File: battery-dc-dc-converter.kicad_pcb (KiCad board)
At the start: 2 copper layers, 42 x 33 mm, 24 parts, among them J1 Conn_01x02, J2 Conn_01x01, J3 Conn_01x01, U1 LMR16030

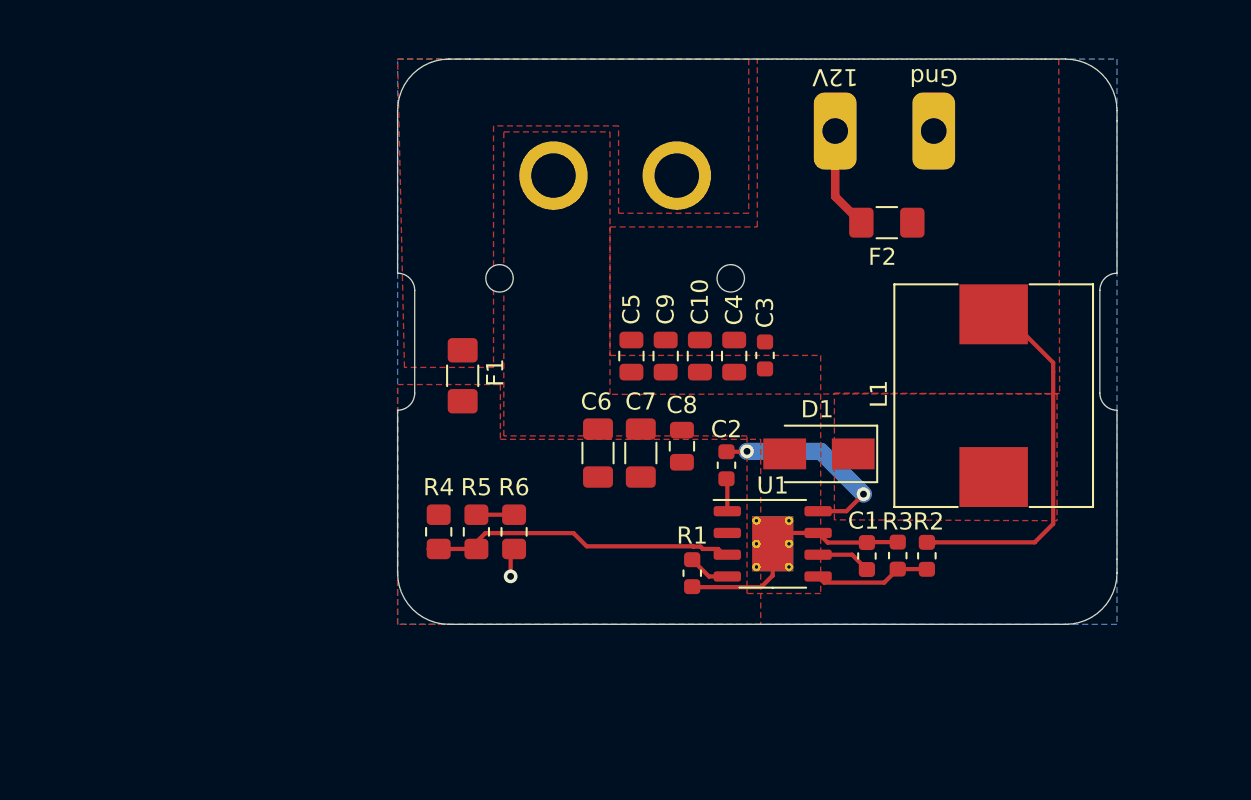
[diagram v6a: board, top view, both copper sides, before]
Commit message: Improved EMI
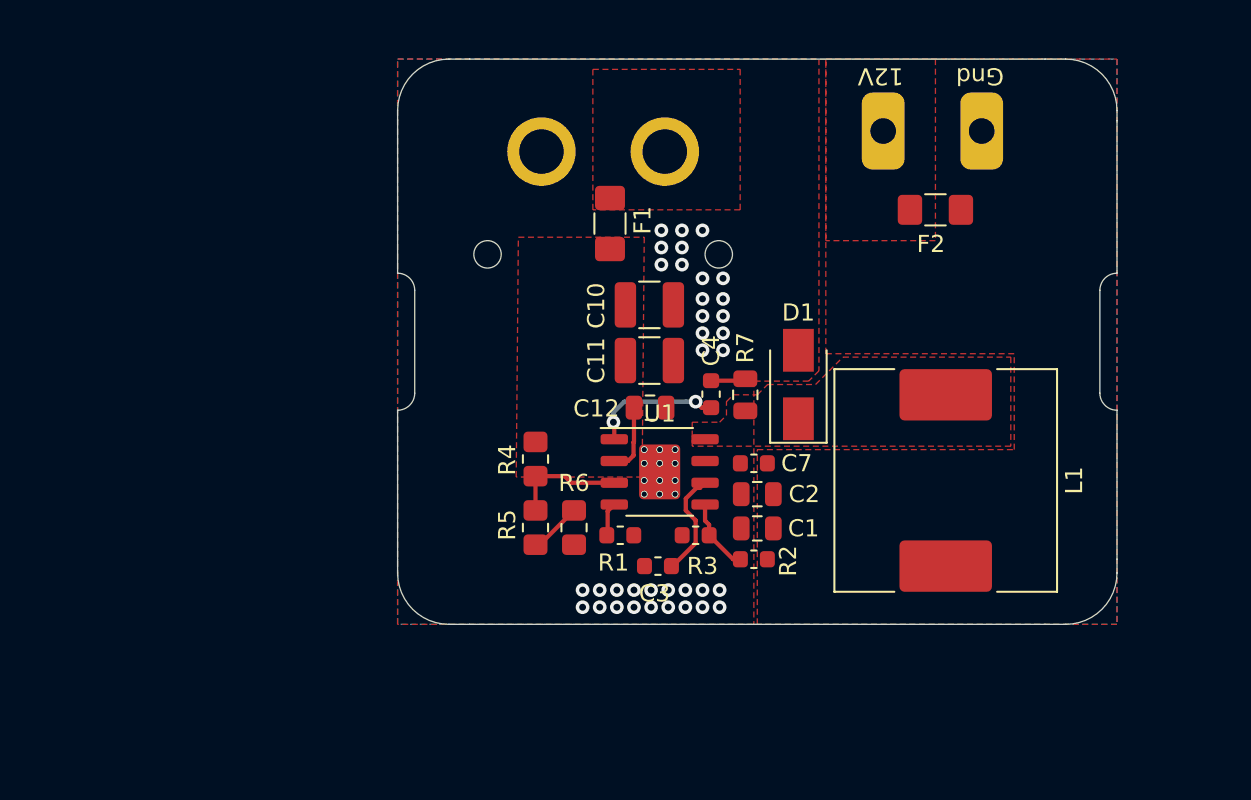
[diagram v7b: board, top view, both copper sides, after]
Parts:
- removed C6: 2.2uF, Capacitor_SMD:C_1206_3216Metric
- removed the C7 at (112.4, 58.2)
- removed C9: 22uF, Capacitor_SMD:C_0805_2012Metric
- added C11: 2.2uF, Capacitor_SMD:C_1210_3225Metric, F.Cu at (112.9, 52.8)
- added R7: 3R3, Resistor_SMD:R_0805_2012Metric, F.Cu at (118.5, 54.8)
- C10: value 22uF -> 2.2uF; footprint Capacitor_SMD:C_0805_2012Metric -> Capacitor_SMD:C_1210_3225Metric
- L1: footprint scooter-ps:MWSA1004 -> battery-dc-dc-converter:SWRH1207B
- U1: footprint Package_SO:HTSOP-8-1EP_3.9x4.9mm_P1.27mm_EP2.4x3.2mm_ThermalVias -> Package_SO:HTSOP-8-1EP_3.9x4.9mm_P1.27mm_EP2.4x3.2mm
- moved F1 12.4 mm to (110.6, 44.8)
- moved C3 12.2 mm to (113.4, 64.8), turned to 180 degrees
- moved R3 11.9 mm to (115.6, 63.0), turned to 180 degrees
- moved C2 10.9 mm to (119.2, 60.6), turned to 180 degrees
- moved C1 10.2 mm to (119.2, 62.6), turned to 180 degrees
- moved R2 10.1 mm to (119.0, 64.4), turned to 180 degrees
- moved U1 7.82 mm to (113.5, 59.3)
- moved R4 7.07 mm to (106.2, 58.5)
- moved C7 6.33 mm to (119.0, 58.8), turned to 180 degrees
- moved L1 5.69 mm to (130.2, 59.8), turned to 270 degrees
- moved R1 4.75 mm to (111.2, 63.0), turned to 0 degrees
- moved C4 4.25 mm to (116.5, 54.8)
- moved D1 4.22 mm to (121.6, 54.2), turned to 90 degrees
- moved C10 4.20 mm to (112.9, 49.5), turned to 0 degrees
- moved R6 3.51 mm to (108.5, 62.5)
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- renumbered C4 to C1, C8 to C12, C5 to C2, C1 to C3, C2 to C4, C3 to C7
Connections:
- C10 pad 1: +12V -> VCC
- C4 pad 1: Net-(C2-Pad1) -> Net-(C4-Pad1)
- D1 pad 1: Net-(C2-Pad1) -> Net-(D1-Pad1)
- L1 pad 1: Net-(C2-Pad1) -> Net-(D1-Pad1)
- U1 pad 8: Net-(C2-Pad1) -> Net-(D1-Pad1)
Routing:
- net +12V: track 21.7 -> 0.00 mm
- net Net-(C2-Pad1): track 12.1 -> 0.00 mm, vias 2 -> 0
- net Net-(R4-Pad2): track 18.5 -> 6.76 mm
- net Net-(F2-Pad1): track 7.09 -> 0.00 mm
- net Net-(C4-Pad2): track 1.92 -> 7.97 mm, vias 0 -> 2
- net VCC: track 0.00 -> 4.06 mm
- net Net-(C3-Pad1): track 3.21 -> 6.31 mm
- net GND: track 16.5 -> 14.0 mm, vias 1 -> 47
- net Net-(R2-Pad2): track 6.83 -> 4.30 mm
- net Net-(C4-Pad1): track 0.00 -> 2.05 mm
- net Net-(R5-Pad2): track 2.40 -> 3.08 mm
- added copper zone on F.Cu, net Net-(D1-Pad1)
- added copper zone on F.Cu, net Net-(F2-Pad1)
- removed copper zone on F.Cu, net Net-(C2-Pad1)

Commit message: Added lmr16020
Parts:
- removed C3: 47nF, Capacitor_SMD:C_0603_1608Metric
- U1: value LMR16030 -> LMR16020
